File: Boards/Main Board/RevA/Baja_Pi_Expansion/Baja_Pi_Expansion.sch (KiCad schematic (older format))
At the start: 10 parts

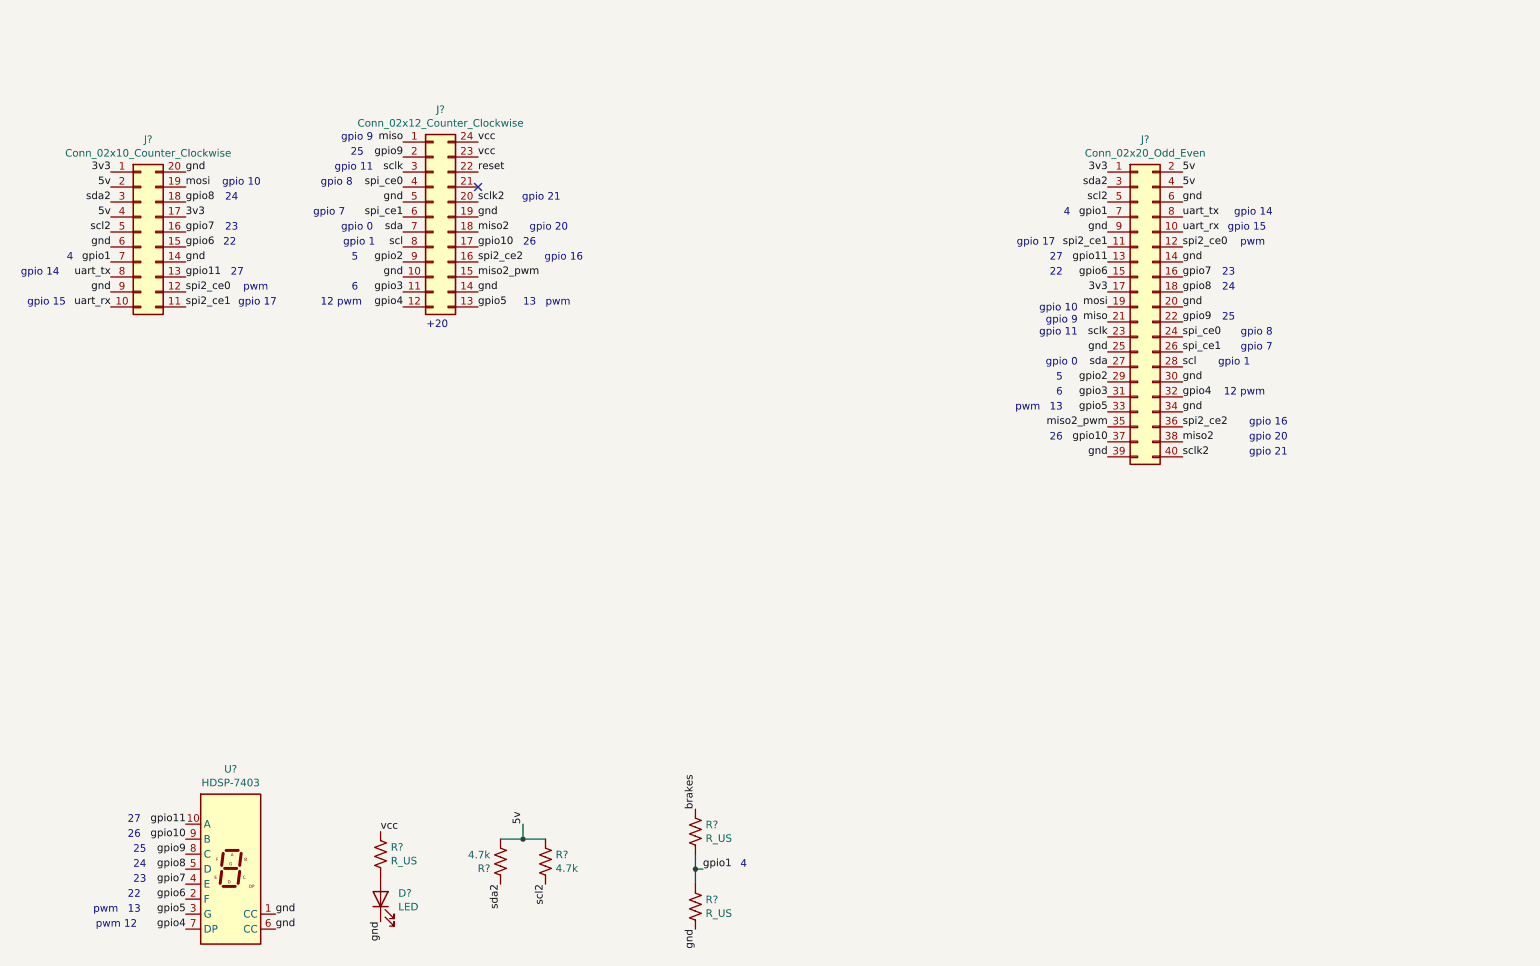
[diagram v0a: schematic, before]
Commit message: Updated Baja_Pi_Expansion with everything but regulator
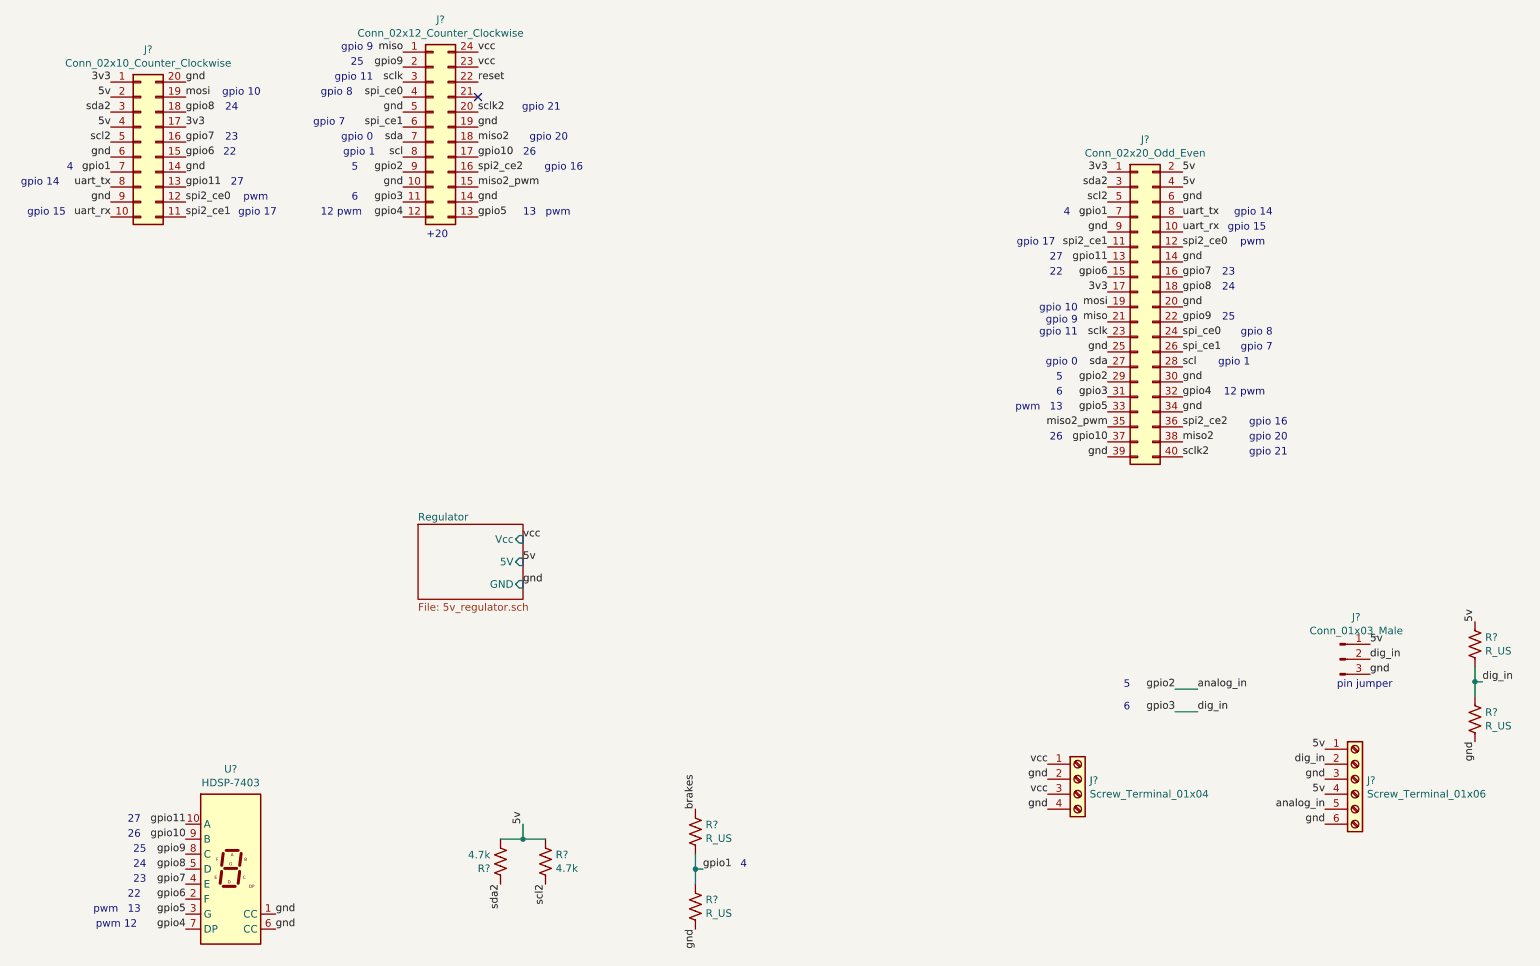
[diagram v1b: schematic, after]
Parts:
- removed D?: LED, symbol Device:LED
- removed R?: R_US, symbol Device:R_US
- added J?: Screw_Terminal_01x06, symbol Connector:Screw_Terminal_01x06
- added J?: Screw_Terminal_01x04, symbol Connector:Screw_Terminal_01x04
- added J?: Conn_01x03_Male, symbol Connector:Conn_01x03_Male
- added R? (x2): R_US, symbol Device:R_US
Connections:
- net 5v: now also J?.1 (Pin_1), J?.1 (Pin_1), J?.4 (Pin_4), R?.1
- net gnd: now also J?.2 (Pin_2), J?.3 (Pin_3), J?.3 (Pin_3), J?.4 (Pin_4), J?.6 (Pin_6), R?.2
- net vcc: now also J?.1 (Pin_1), J?.3 (Pin_3)
- net gpio2 renamed analog_in
- net analog_in: now also J?.5 (Pin_5)
- net gpio3 renamed dig_in
- net dig_in: now also J?.2 (Pin_2), J?.2 (Pin_2), R?.1, R?.2
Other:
- note added: "pin jumper"
- moved on the sheet: J?
